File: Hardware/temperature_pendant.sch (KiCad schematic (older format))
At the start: 6 parts, among them J1 CONN-6, SW1 SW-MOM, U1 BLINKM/MINM, U2 TMP3X

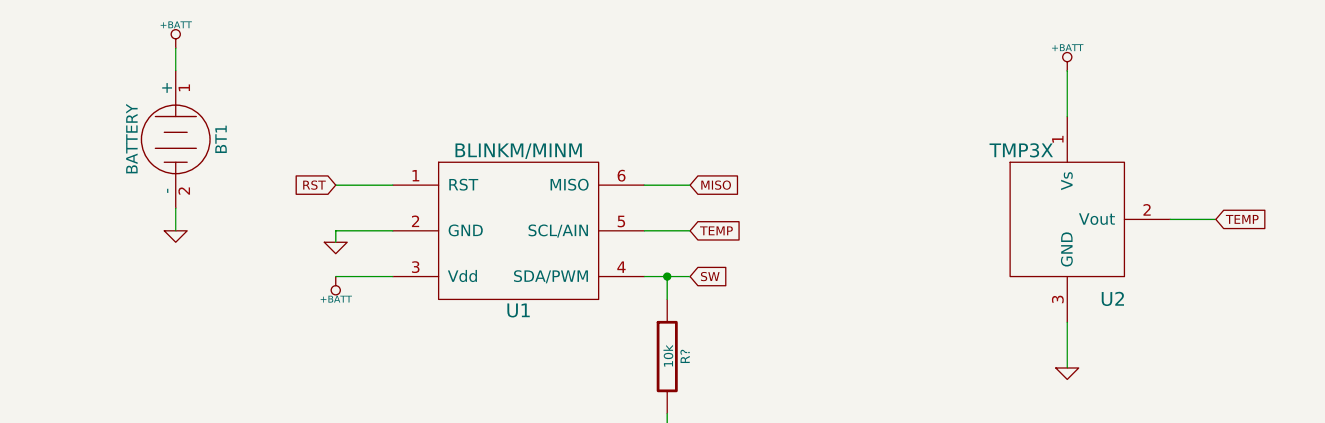
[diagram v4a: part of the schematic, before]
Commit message: Fixed issues
Fixed several issues.  In the schematic added pull-down resistor and
also some caps to improve performance and noise issues.  Re-wrote the
temperature reading routine and color picking.  Enabled the internal
voltage reference and set to 2.56 VDC reference voltage.  This means the
values won't change as the battery voltage drops over time.  Cleaned up
various parts of the code.  Tested to work so far on the rev1 boards.
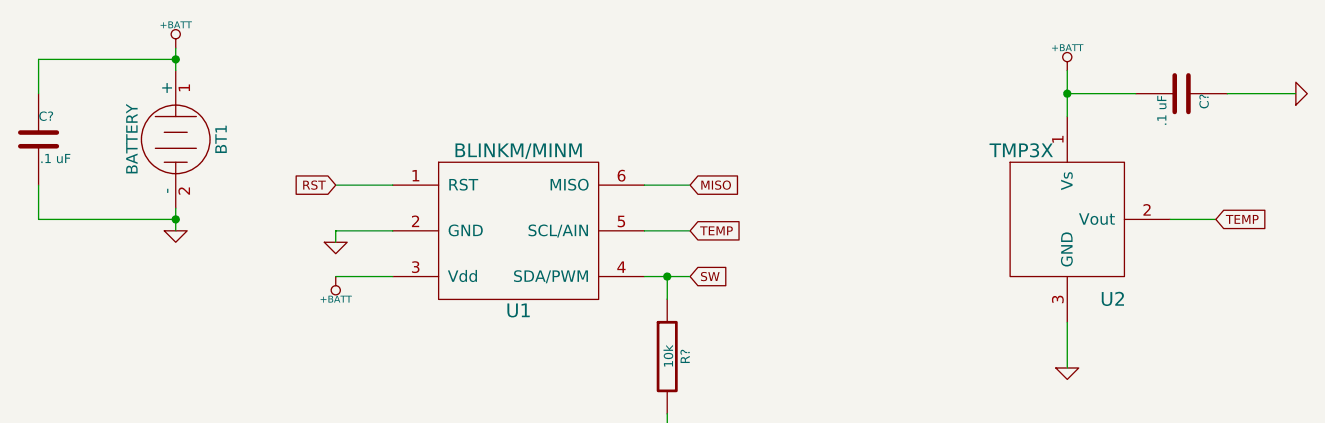
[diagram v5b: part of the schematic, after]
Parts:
- added C? (x2): .1 uF, ~, symbol C
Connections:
- net +BATT: now also C?.1, C?.2
- net GND: now also C?.1, C?.2
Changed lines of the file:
@@
 Sheet 1 1
 Title "Temperature Pendant"
-Date "7 dec 2013"
+Date "8 dec 2013"
 Rev "1"
 Comp "Matthew E. Nelson"
@@
 	1    0    0    -1
 $EndComp
+$Comp
+L C C?
+U 1 1 52A4A502
+P 8400 3000
+F 0 "C?" H 8400 3100 40  0000 L CNN
+F 1 ".1 uF" H 8406 2915 40  0000 L CNN
+F 2 "~" H 8438 2850 30  0000 C CNN
+F 3 "~" H 8400 3000 60  0000 C CNN
+	1    8400 3000
+	0    1    1    0
+$EndComp
+Wire Wire Line
+	8200 3000 7900 3000
+Connection ~ 7900 3000
+Wire Wire Line
+	8600 3000 8900 3000
+$Comp
+L GND #PWR?
+U 1 1 52A4A54D
+P 8900 3000
+F 0 "#PWR?" H 8900 3000 30  0001 C CNN
+F 1 "GND" H 8900 2930 30  0001 C CNN
+F 2 "" H 8900 3000 60  0000 C CNN
+F 3 "" H 8900 3000 60  0000 C CNN
+	1    8900 3000
+	0    -1   -1   0
+$EndComp
+$Comp
+L C C?
+U 1 1 52A4B732
+P 3400 3200
+F 0 "C?" H 3400 3300 40  0000 L CNN
+F 1 ".1 uF" H 3406 3115 40  0000 L CNN
+F 2 "~" H 3438 3050 30  0000 C CNN
+F 3 "~" H 3400 3200 60  0000 C CNN
+	1    3400 3200
+	1    0    0    -1
+$EndComp
+Wire Wire Line
+	3400 3000 3400 2850
+Wire Wire Line
+	3400 2850 4000 2850
+Connection ~ 4000 2850
+Wire Wire Line
+	3400 3400 3400 3550
+Wire Wire Line
+	3400 3550 4000 3550
+Connection ~ 4000 3550
 $EndSCHEMATC

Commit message: Minor update
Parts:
- gave numbers to parts that had none: 3
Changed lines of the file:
@@
 Sheet 1 1
 Title "Temperature Pendant"
-Date "8 dec 2013"
+Date "9 dec 2013"
 Rev "1"
 Comp "Matthew E. Nelson"
@@
 $EndComp
 $Comp
-L R R?
+L R R1
 U 1 1 52A2BDC6
 P 6150 4150
-F 0 "R?" V 6230 4150 40  0000 C CNN
+F 0 "R1" V 6230 4150 40  0000 C CNN
 F 1 "10k" V 6157 4151 40  0000 C CNN
 F 2 "~" V 6080 4150 30  0000 C CNN
@@
 	6150 4400 6150 4550
 $Comp
-L GND #PWR?
+L GND #PWR010
 U 1 1 52A2BE02
 P 6150 4550
-F 0 "#PWR?" H 6150 4550 30  0001 C CNN
+F 0 "#PWR010" H 6150 4550 30  0001 C CNN
 F 1 "GND" H 6150 4480 30  0001 C CNN
 F 2 "" H 6150 4550 60  0000 C CNN
@@
 $EndComp
 $Comp
-L C C?
+L C C2
 U 1 1 52A4A502
 P 8400 3000
-F 0 "C?" H 8400 3100 40  0000 L CNN
+F 0 "C2" H 8400 3100 40  0000 L CNN
 F 1 ".1 uF" H 8406 2915 40  0000 L CNN
 F 2 "~" H 8438 2850 30  0000 C CNN
@@
 	8600 3000 8900 3000
 $Comp
-L GND #PWR?
+L GND #PWR011
 U 1 1 52A4A54D
 P 8900 3000
-F 0 "#PWR?" H 8900 3000 30  0001 C CNN
+F 0 "#PWR011" H 8900 3000 30  0001 C CNN
 F 1 "GND" H 8900 2930 30  0001 C CNN
 F 2 "" H 8900 3000 60  0000 C CNN
@@
 $EndComp
 $Comp
-L C C?
+L C C1
 U 1 1 52A4B732
 P 3400 3200
-F 0 "C?" H 3400 3300 40  0000 L CNN
+F 0 "C1" H 3400 3300 40  0000 L CNN
 F 1 ".1 uF" H 3406 3115 40  0000 L CNN
 F 2 "~" H 3438 3050 30  0000 C CNN

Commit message: Added MCP73831 Charger
Deceided to design around using a 3.7 Li-Poly flat pack battery.  To
make it more user friendly (ie don't need to fumble getting the battery
out) I have added a MCP73831 Charger.  Currently set to 500 mA charge.
This should be fine for any Li-Poly battery that has a maximum voltage
of 4.2 and a minimum capacity of 500 mAh.  Batteries with smaller
capacity may be damaged by the higher charge current as most batteries
are a 1C charge rate.
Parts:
- added C2: 4.7uF, ~, symbol C
- added D1: LED, ~, symbol LED
- added J2: USB_MINI, ~, symbol USB_MINI
- added R1: 330, ~, symbol R
- added R2: 2K, ~, symbol R
- added U1: MCP73831/2, symbol MCP73831/2
- renumbered C2 to C3, R1 to R3, U1 to U2, U2 to U3
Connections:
- wire segments 28 -> 45
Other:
- moved on the sheet: BT1, C1
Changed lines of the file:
@@
 Sheet 1 1
 Title "Temperature Pendant"
-Date "9 dec 2013"
+Date "11 jan 2014"
 Rev "1"
 Comp "Matthew E. Nelson"
@@
 L BATTERY BT1
 U 1 1 5264A202
-P 4000 3200
-F 0 "BT1" H 4000 3400 50  0000 C CNN
-F 1 "BATTERY" H 4000 3010 50  0000 C CNN
-F 2 "~" H 4000 3200 60  0000 C CNN
-F 3 "~" H 4000 3200 60  0000 C CNN
-	1    4000 3200
+P 3150 2950
+F 0 "BT1" H 3150 3150 50  0000 C CNN
+F 1 "BATTERY" H 3150 2760 50  0000 C CNN
+F 2 "~" H 3150 2950 60  0000 C CNN
+F 3 "~" H 3150 2950 60  0000 C CNN
+	1    3150 2950
 	0    1    1    0
 $EndComp
 $Comp
-L TMP3X U2
+L TMP3X U3
 U 1 1 5264B6FD
 P 7900 3550
-F 0 "U2" H 8100 3200 60  0000 C CNN
+F 0 "U3" H 8100 3200 60  0000 C CNN
 F 1 "TMP3X" H 7700 3850 60  0000 C CNN
 F 2 "" H 7900 3550 60  0000 C CNN
@@
 $EndComp
 $Comp
-L BLINKM/MINM U1
+L BLINKM/MINM U2
 U 1 1 5265EB43
 P 5500 3700
-F 0 "U1" H 5500 3450 60  0000 C CNN
+F 0 "U2" H 5500 3450 60  0000 C CNN
 F 1 "BLINKM/MINM" H 5500 4150 60  0000 C CNN
 F 2 "" H 5500 3700 60  0000 C CNN
@@
 	1    0    0    -1
 $EndComp
-Wire Wire Line
-	4000 3500 4000 3600
 $Comp
 L GND #PWR01
 U 1 1 5265EE24
-P 4000 3600
-F 0 "#PWR01" H 4000 3600 30  0001 C CNN
-F 1 "GND" H 4000 3530 30  0001 C CNN
-F 2 "" H 4000 3600 60  0000 C CNN
-F 3 "" H 4000 3600 60  0000 C CNN
-	1    4000 3600
-	1    0    0    -1
-$EndComp
-Wire Wire Line
-	4000 2900 4000 2800
+P 3350 3350
+F 0 "#PWR01" H 3350 3350 30  0001 C CNN
+F 1 "GND" H 3350 3280 30  0001 C CNN
+F 2 "" H 3350 3350 60  0000 C CNN
+F 3 "" H 3350 3350 60  0000 C CNN
+	1    3350 3350
+	1    0    0    -1
+$EndComp
 $Comp
 L +BATT #PWR02
 U 1 1 5265EE65
-P 4000 2800
-F 0 "#PWR02" H 4000 2750 20  0001 C CNN
-F 1 "+BATT" H 4000 2900 30  0000 C CNN
-F 2 "" H 4000 2800 60  0000 C CNN
-F 3 "" H 4000 2800 60  0000 C CNN
-	1    4000 2800
+P 3350 2550
+F 0 "#PWR02" H 3350 2500 20  0001 C CNN
+F 1 "+BATT" H 3350 2650 30  0000 C CNN
+F 2 "" H 3350 2550 60  0000 C CNN
+F 3 "" H 3350 2550 60  0000 C CNN
+	1    3350 2550
 	1    0    0    -1
 $EndComp
@@
 $EndComp
 $Comp
-L R R1
+L R R3
 U 1 1 52A2BDC6
 P 6150 4150
-F 0 "R1" V 6230 4150 40  0000 C CNN
+F 0 "R3" V 6230 4150 40  0000 C CNN
 F 1 "10k" V 6157 4151 40  0000 C CNN
 F 2 "~" V 6080 4150 30  0000 C CNN
@@
 $EndComp
 $Comp
-L C C2
+L C C3
 U 1 1 52A4A502
 P 8400 3000
-F 0 "C2" H 8400 3100 40  0000 L CNN
+F 0 "C3" H 8400 3100 40  0000 L CNN
 F 1 ".1 uF" H 8406 2915 40  0000 L CNN
 F 2 "~" H 8438 2850 30  0000 C CNN
@@
 L C C1
 U 1 1 52A4B732
-P 3400 3200
-F 0 "C1" H 3400 3300 40  0000 L CNN
-F 1 ".1 uF" H 3406 3115 40  0000 L CNN
-F 2 "~" H 3438 3050 30  0000 C CNN
-F 3 "~" H 3400 3200 60  0000 C CNN
-	1    3400 3200
-	1    0    0    -1
-$EndComp
-Wire Wire Line
-	3400 3000 3400 2850
-Wire Wire Line
-	3400 2850 4000 2850
-Connection ~ 4000 2850
-Wire Wire Line
-	3400 3400 3400 3550
-Wire Wire Line
-	3400 3550 4000 3550
-Connection ~ 4000 3550
+P 2750 2950
+F 0 "C1" H 2750 3050 40  0000 L CNN
+F 1 ".1 uF" H 2756 2865 40  0000 L CNN
+F 2 "~" H 2788 2800 30  0000 C CNN
+F 3 "~" H 2750 2950 60  0000 C CNN
+	1    2750 2950
+	1    0    0    -1
+$EndComp
+Wire Wire Line
+	3350 2650 3350 2550
+Connection ~ 3350 2650
+Wire Wire Line
+	2750 2750 2750 2650
+Connection ~ 3150 2650
+Wire Wire Line
+	2750 3150 2750 3250
+Connection ~ 3150 3250
+Wire Wire Line
+	3350 3350 3350 3250
+Connection ~ 3350 3250
+$Comp
+L MCP73831/2 U1
+U 1 1 52D1B0BC
+P 3250 1500
+F 0 "U1" H 3250 2000 60  0000 C CNN
+F 1 "MCP73831/2" H 3250 950 60  0000 C CNN
+F 2 "" H 3250 1500 60  0000 C CNN
+F 3 "" H 3250 1500 60  0000 C CNN
+	1    3250 1500
+	1    0    0    -1
+$EndComp
+$Comp
+L USB_MINI J2
+U 1 1 52D1B0CB
+P 5350 1400
+F 0 "J2" H 5350 1700 60  0000 C CNN
+F 1 "USB_MINI" H 5350 1000 60  0000 C CNN
+F 2 "~" H 5350 1400 60  0000 C CNN
+F 3 "~" H 5350 1400 60  0000 C CNN
+	1    5350 1400
+	1    0    0    -1
+$EndComp
+Wire Wire Line
+	5050 1250 3900 1250
+$Comp
+L GND #PWR012
+U 1 1 52D1B105
+P 4900 1750
+F 0 "#PWR012" H 4900 1750 30  0001 C CNN
+F 1 "GND" H 4900 1680 30  0001 C CNN
+F 2 "" H 4900 1750 60  0000 C CNN
+F 3 "" H 4900 1750 60  0000 C CNN
+	1    4900 1750
+	1    0    0    -1
+$EndComp
+Wire Wire Line
+	5050 1650 4900 1650
+Wire Wire Line
+	4900 1650 4900 1750
+$Comp
+L GND #PWR013
+U 1 1 52D1B155
+P 2500 1600
+F 0 "#PWR013" H 2500 1600 30  0001 C CNN
+F 1 "GND" H 2500 1530 30  0001 C CNN
+F 2 "" H 2500 1600 60  0000 C CNN
+F 3 "" H 2500 1600 60  0000 C CNN
+	1    2500 1600
+	1    0    0    -1
+$EndComp
+Wire Wire Line
+	2600 1500 2500 1500
+Wire Wire Line
+	2500 1500 2500 1600
+$Comp
+L LED D1
+U 1 1 52D1B183
+P 2200 1200
+F 0 "D1" H 2200 1300 50  0000 C CNN
+F 1 "LED" H 2200 1100 50  0000 C CNN
+F 2 "~" H 2200 1200 60  0000 C CNN
+F 3 "~" H 2200 1200 60  0000 C CNN
+	1    2200 1200
+	1    0    0    -1
+$EndComp
+$Comp
+L R R1
+U 1 1 52D1B1B0
+P 1550 1200
+F 0 "R1" V 1630 1200 40  0000 C CNN
+F 1 "330" V 1557 1201 40  0000 C CNN
+F 2 "~" V 1480 1200 30  0000 C CNN
+F 3 "~" H 1550 1200 30  0000 C CNN
+	1    1550 1200
+	0    1    1    0
+$EndComp
+Wire Wire Line
+	1800 1200 2000 1200
+Wire Wire Line
+	2400 1200 2600 1200
+Wire Wire Line
+	1300 1200 1300 900
+Wire Wire Line
+	1300 900  4050 900
+Wire Wire Line
+	4050 900  4050 1250
+Connection ~ 4050 1250
+$Comp
+L R R2
+U 1 1 52D1B240
+P 4100 2000
+F 0 "R2" V 4180 2000 40  0000 C CNN
+F 1 "2K" V 4107 2001 40  0000 C CNN
+F 2 "~" V 4030 2000 30  0000 C CNN
+F 3 "~" H 4100 2000 30  0000 C CNN
+	1    4100 2000
+	1    0    0    -1
+$EndComp
+Wire Wire Line
+	3900 1750 4100 1750
+$Comp
+L GND #PWR014
+U 1 1 52D1B280
+P 4100 2400
+F 0 "#PWR014" H 4100 2400 30  0001 C CNN
+F 1 "GND" H 4100 2330 30  0001 C CNN
+F 2 "" H 4100 2400 60  0000 C CNN
+F 3 "" H 4100 2400 60  0000 C CNN
+	1    4100 2400
+	1    0    0    -1
+$EndComp
+Wire Wire Line
+	4100 2250 4100 2400
+Wire Wire Line
+	2600 1800 2600 2350
+Wire Wire Line
+	2600 2350 3150 2350
+Wire Wire Line
+	3150 2350 3150 2650
+Wire Wire Line
+	2750 2650 3350 2650
+Wire Wire Line
+	3350 3250 2750 3250
+$Comp
+L C C2
+U 1 1 52D1B3B5
+P 4650 1500
+F 0 "C2" H 4650 1600 40  0000 L CNN
+F 1 "4.7uF" H 4656 1415 40  0000 L CNN
+F 2 "~" H 4688 1350 30  0000 C CNN
+F 3 "~" H 4650 1500 60  0000 C CNN
+	1    4650 1500
+	1    0    0    -1
+$EndComp
+Wire Wire Line
+	4650 1300 4650 1250
+Connection ~ 4650 1250
+Wire Wire Line
+	4650 1700 4900 1700
+Connection ~ 4900 1700
 $EndSCHEMATC
